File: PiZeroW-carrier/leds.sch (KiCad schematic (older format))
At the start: 10 parts

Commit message: netlist update and read into pcb
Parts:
- D1, D2, D3, D4, D5: footprint HerbsParts:LED_RGB_5050-6 -> lib_fp:5050; symbol LED_RGB -> LED_RGB-RESCUE-PiZeroW-carrier
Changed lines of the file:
@@
 EESchema Schematic File Version 2
+LIBS:PiZeroW-carrier-rescue
 LIBS:power
 LIBS:device
@@
 $EndDescr
 $Comp
-L LED_RGB D1
+L LED_RGB-RESCUE-PiZeroW-carrier D1
 U 1 1 5A215909
 P 1950 1715
 F 0 "D1" H 1950 2140 50  0000 C CNN
 F 1 "LED_QBLP679E" H 1950 2065 50  0000 C CNN
-F 2 "HerbsParts:LED_RGB_5050-6" H 2080 1305 50  0001 C CNN
+F 2 "lib_fp:5050" H 2080 1305 50  0001 C CNN
 F 3 "QBLP679E-IGK" H 1950 1665 50  0001 C CNN
 	1    1950 1715
@@
 GND
 $Comp
-L LED_RGB D2
+L LED_RGB-RESCUE-PiZeroW-carrier D2
 U 1 1 5A258F33
 P 3745 1745
 F 0 "D2" H 3745 2170 50  0000 C CNN
 F 1 "LED_QBLP679E" H 3745 2095 50  0000 C CNN
-F 2 "HerbsParts:LED_RGB_5050-6" H 3875 1335 50  0001 C CNN
+F 2 "lib_fp:5050" H 3875 1335 50  0001 C CNN
 F 3 "QBLP679E-IGK" H 3745 1695 50  0001 C CNN
 	1    3745 1745
@@
 GND
 $Comp
-L LED_RGB D3
+L LED_RGB-RESCUE-PiZeroW-carrier D3
 U 1 1 5A259049
 P 5575 1770
 F 0 "D3" H 5575 2195 50  0000 C CNN
 F 1 "LED_QBLP679E" H 5575 2120 50  0000 C CNN
-F 2 "HerbsParts:LED_RGB_5050-6" H 5705 1360 50  0001 C CNN
+F 2 "lib_fp:5050" H 5705 1360 50  0001 C CNN
 F 3 "QBLP679E-IGK" H 5575 1720 50  0001 C CNN
 	1    5575 1770
@@
 GND
 $Comp
-L LED_RGB D4
+L LED_RGB-RESCUE-PiZeroW-carrier D4
 U 1 1 5A259067
 P 7370 1800
 F 0 "D4" H 7370 2225 50  0000 C CNN
 F 1 "LED_QBLP679E" H 7370 2150 50  0000 C CNN
-F 2 "HerbsParts:LED_RGB_5050-6" H 7500 1390 50  0001 C CNN
+F 2 "lib_fp:5050" H 7500 1390 50  0001 C CNN
 F 3 "QBLP679E-IGK" H 7370 1750 50  0001 C CNN
 	1    7370 1800
@@
 GND
 $Comp
-L LED_RGB D5
+L LED_RGB-RESCUE-PiZeroW-carrier D5
 U 1 1 5A259105
 P 9160 1770
 F 0 "D5" H 9160 2195 50  0000 C CNN
 F 1 "LED_QBLP679E" H 9160 2120 50  0000 C CNN
-F 2 "HerbsParts:LED_RGB_5050-6" H 9290 1360 50  0001 C CNN
+F 2 "lib_fp:5050" H 9290 1360 50  0001 C CNN
 F 3 "QBLP679E-IGK" H 9160 1720 50  0001 C CNN
 	1    9160 1770

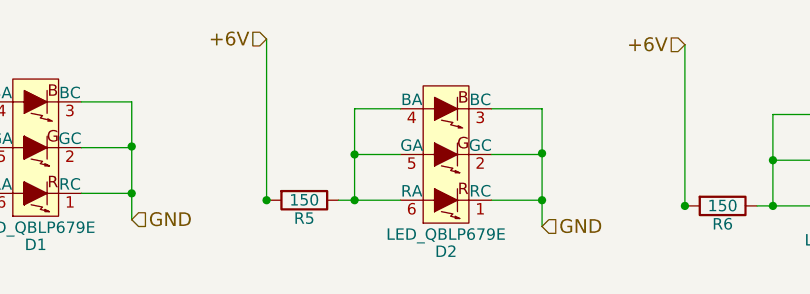
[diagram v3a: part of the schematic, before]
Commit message: Before Trace fix of LED AND PIDISABLE
Push before tracing fix of LEDEnable and PIDisable
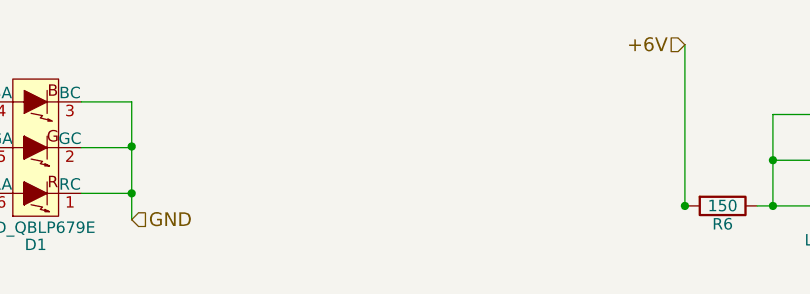
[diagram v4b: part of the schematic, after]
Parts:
- removed D2: LED_QBLP679E, lib_fp:5050, symbol LED_RGB-RESCUE-PiZeroW-carrier
- removed R5: 150, Resistors_SMD:R_1206_HandSoldering, symbol R
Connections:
- wire segments 55 -> 44
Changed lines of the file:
@@
-GND
-$Comp
-L LED_RGB-RESCUE-PiZeroW-carrier D2
-U 1 1 5A258F33
-P 3745 1745
-F 0 "D2" H 3745 2170 50  0000 C CNN
-F 1 "LED_QBLP679E" H 3745 2095 50  0000 C CNN
-F 2 "lib_fp:5050" H 3875 1335 50  0001 C CNN
-F 3 "QBLP679E-IGK" H 3745 1695 50  0001 C CNN
-	1    3745 1745
-	-1   0    0    1
-$EndComp
-Wire Wire Line
-	4165 1545 4165 2060
-Wire Wire Line
-	4165 1945 3945 1945
-$Comp
-L R R5
-U 1 1 5A258F3B
-P 3125 1945
-F 0 "R5" V 3205 1945 50  0000 C CNN
-F 1 "150" V 3125 1945 50  0000 C CNN
-F 2 "Resistors_SMD:R_1206_HandSoldering" V 3055 1945 50  0001 C CNN
-F 3 "" H 3125 1945 50  0000 C CNN
-	1    3125 1945
-	0    1    1    0
-$EndComp
-Wire Wire Line
-	3275 1945 3545 1945
-Wire Wire Line
-	2955 1945 2975 1945
-Wire Wire Line
-	3945 1545 4165 1545
-Connection ~ 4165 1945
-Wire Wire Line
-	3945 1745 4165 1745
-Wire Wire Line
-	4165 1745 4165 1740
-Connection ~ 4165 1740
-Wire Wire Line
-	3545 1545 3345 1545
-Wire Wire Line
-	3345 1545 3345 1945
-Connection ~ 3345 1945
-Wire Wire Line
-	3345 1745 3545 1745
-Connection ~ 3345 1745
-Wire Wire Line
-	2960 1240 2960 1945
-Connection ~ 2960 1945
-Text HLabel 2960 1240 0    60   Input ~ 0
-+6V
-Text HLabel 4165 2060 2    60   Input ~ 0
 GND
 $Comp
